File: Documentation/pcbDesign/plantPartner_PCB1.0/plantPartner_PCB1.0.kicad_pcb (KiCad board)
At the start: 2 copper layers, 1 part, among them U1 ESP32-WROOM-32

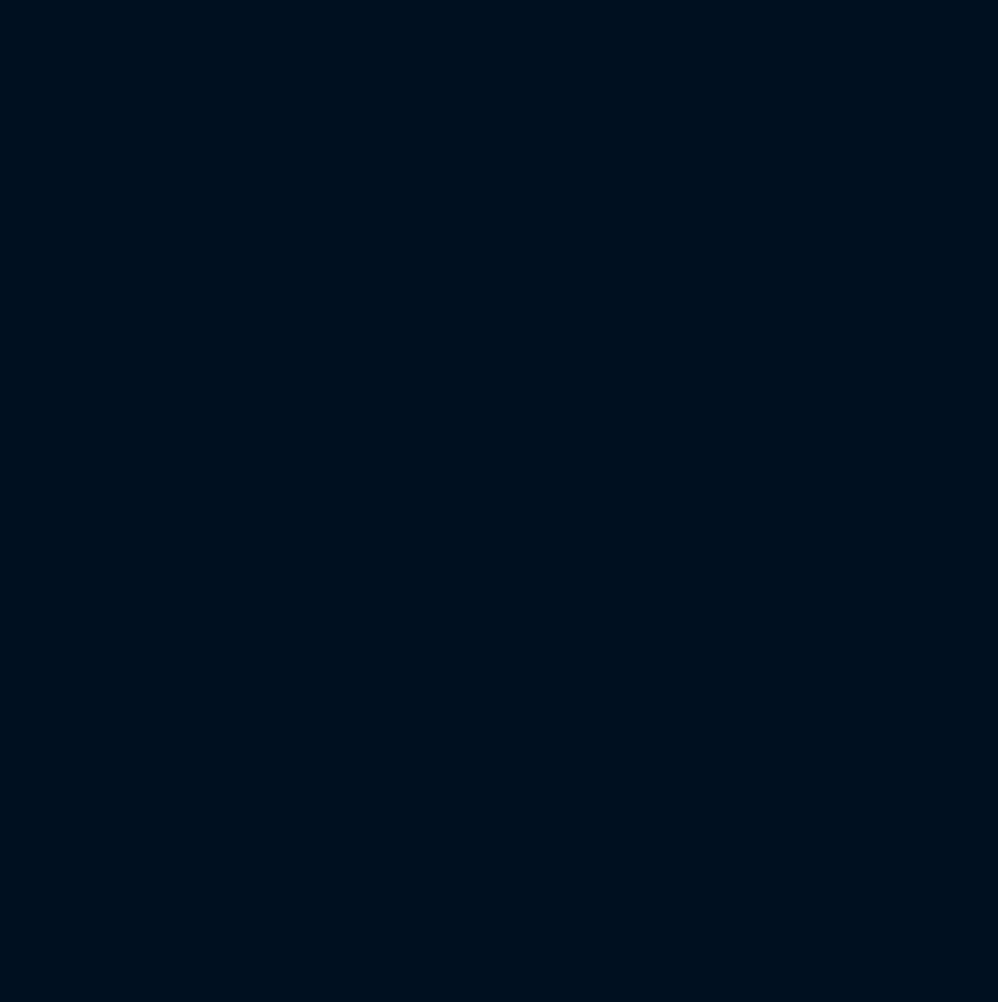
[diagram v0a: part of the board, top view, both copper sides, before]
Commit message: Verified the Schematic designs for the RS-485 Transceiver and Buck Converter. I will verify the 5V Relay next and then start routing the PCB itself ASAP
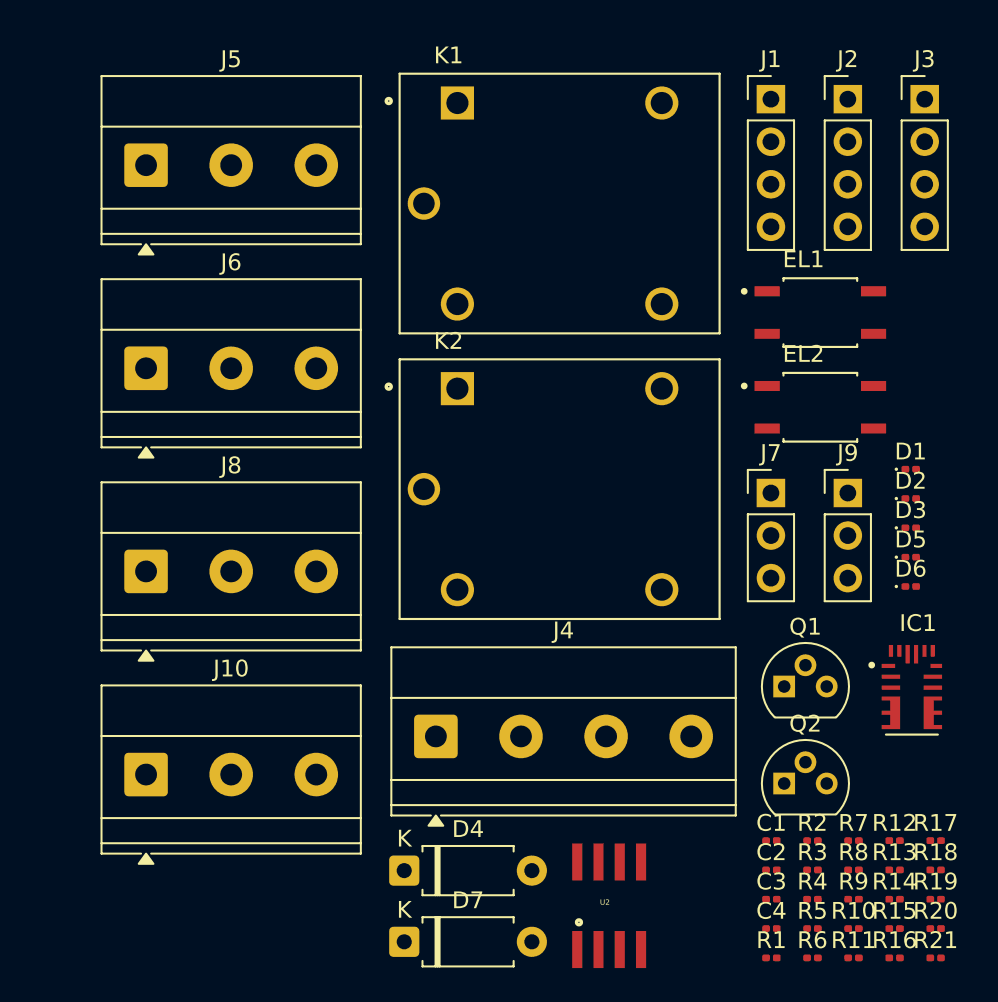
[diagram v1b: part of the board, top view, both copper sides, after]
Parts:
- added C1: 22uF, Capacitor_SMD:C_0201_0603Metric, F.Cu at (163.4, 86.0)
- added C2: 22uF, Capacitor_SMD:C_0201_0603Metric, F.Cu at (163.4, 87.8)
- added C3: 10uF, Capacitor_SMD:C_0201_0603Metric, F.Cu at (163.4, 89.5)
- added C4: 0.1uF, Capacitor_SMD:C_0201_0603Metric, F.Cu at (163.4, 91.2)
- added D1: LED, LED_SMD:LED_0201_0603Metric, F.Cu at (171.7, 63.8)
- added D2: LED, LED_SMD:LED_0201_0603Metric, F.Cu at (171.7, 65.6)
- added D3: LED, LED_SMD:LED_0201_0603Metric, F.Cu at (171.7, 67.3)
- added D4: 1N400x, Diode_THT:D_A-405_P7.62mm_Horizontal, F.Cu at (141.4, 87.8)
- added D5: LED, LED_SMD:LED_0201_0603Metric, F.Cu at (171.7, 69.1)
- added D6: LED, LED_SMD:LED_0201_0603Metric, F.Cu at (171.7, 70.8)
- added D7: 1N400x, Diode_THT:D_A-405_P7.62mm_Horizontal, F.Cu at (141.4, 92.0)
- added EL1: ~, MyCustomFootprints:OPTO_EL357N-G, F.Cu at (166.3, 54.5)
- added EL2: ~, MyCustomFootprints:OPTO_EL357N-G, F.Cu at (166.3, 60.1)
- added IC1: MPM3610, MyCustomFootprints:CONV_MPM3610GQV-P, F.Cu at (171.7, 77.1)
- added J1: Conn_01x04, Connector_PinHeader_2.54mm:PinHeader_1x04_P2.54mm_Vertical, F.Cu at (163.3, 41.7)
- added J10: Screw_Terminal, TerminalBlock_Phoenix:TerminalBlock_Phoenix_MKDS-1,5-3-5.08_1x03_P5.08mm_Horizontal, F.Cu at (126.0, 82.1)
- added J2: Conn_01x04, Connector_PinHeader_2.54mm:PinHeader_1x04_P2.54mm_Vertical, F.Cu at (167.9, 41.7)
- added J3: Conn_01x04, Connector_PinHeader_2.54mm:PinHeader_1x04_P2.54mm_Vertical, F.Cu at (172.5, 41.7)
- added J4: Screw_Terminal, TerminalBlock_Phoenix:TerminalBlock_Phoenix_MKDS-1,5-4-5.08_1x04_P5.08mm_Horizontal, F.Cu at (143.3, 79.8)
- added J5: Screw_Terminal, TerminalBlock_Phoenix:TerminalBlock_Phoenix_MKDS-1,5-3-5.08_1x03_P5.08mm_Horizontal, F.Cu at (126.0, 45.7)
- added J6: Screw_Terminal, TerminalBlock_Phoenix:TerminalBlock_Phoenix_MKDS-1,5-3-5.08_1x03_P5.08mm_Horizontal, F.Cu at (126.0, 57.8)
- added J7: Conn_01x03, Connector_PinHeader_2.54mm:PinHeader_1x03_P2.54mm_Vertical, F.Cu at (163.3, 65.2)
- added J8: Screw_Terminal, TerminalBlock_Phoenix:TerminalBlock_Phoenix_MKDS-1,5-3-5.08_1x03_P5.08mm_Horizontal, F.Cu at (126.0, 69.9)
- added J9: Conn_01x03, Connector_PinHeader_2.54mm:PinHeader_1x03_P2.54mm_Vertical, F.Cu at (167.9, 65.2)
- added K1: SRD-05VDC-SL-C, MyCustomFootprints:RELAY_SRD-05VDC-SL-C, F.Cu at (150.7, 48.0)
- added K2: SRD-05VDC-SL-C, MyCustomFootprints:RELAY_SRD-05VDC-SL-C, F.Cu at (150.7, 65.0)
- added Q1: PNP, Package_TO_SOT_THT:TO-92, F.Cu at (164.1, 76.8)
- added Q2: PNP, Package_TO_SOT_THT:TO-92, F.Cu at (164.1, 82.6)
- added R1: 100k, Resistor_SMD:R_0201_0603Metric, F.Cu at (163.4, 93.0)
- added R10: 20k, Resistor_SMD:R_0201_0603Metric, F.Cu at (168.3, 91.2)
- added R11: 120, Resistor_SMD:R_0201_0603Metric, F.Cu at (168.3, 93.0)
- added R12: 1k, Resistor_SMD:R_0201_0603Metric, F.Cu at (170.7, 86.0)
- added R13: 500, Resistor_SMD:R_0201_0603Metric, F.Cu at (170.7, 87.8)
- added R14: 10k, Resistor_SMD:R_0201_0603Metric, F.Cu at (170.7, 89.5)
- added R15: 470, Resistor_SMD:R_0201_0603Metric, F.Cu at (170.7, 91.2)
- added R16: 1k, Resistor_SMD:R_0201_0603Metric, F.Cu at (170.7, 93.0)
- added R17: 1k, Resistor_SMD:R_0201_0603Metric, F.Cu at (173.2, 86.0)
- added R18: 500, Resistor_SMD:R_0201_0603Metric, F.Cu at (173.2, 87.8)
- added R19: 10k, Resistor_SMD:R_0201_0603Metric, F.Cu at (173.2, 89.5)
- added R2: 100k, Resistor_SMD:R_0201_0603Metric, F.Cu at (165.8, 86.0)
- added R20: 470, Resistor_SMD:R_0201_0603Metric, F.Cu at (173.2, 91.2)
- added R21: 1k, Resistor_SMD:R_0201_0603Metric, F.Cu at (173.2, 93.0)
- added R3: 18.7k, Resistor_SMD:R_0201_0603Metric, F.Cu at (165.8, 87.8)
- added R4: 10k, Resistor_SMD:R_0201_0603Metric, F.Cu at (165.8, 89.5)
- added R5: 10k, Resistor_SMD:R_0201_0603Metric, F.Cu at (165.8, 91.2)
- added R6: 10k, Resistor_SMD:R_0201_0603Metric, F.Cu at (165.8, 93.0)
- added R7: 10k, Resistor_SMD:R_0201_0603Metric, F.Cu at (168.3, 86.0)
- added R8: 1k, Resistor_SMD:R_0201_0603Metric, F.Cu at (168.3, 87.8)
- added R9: 20k, Resistor_SMD:R_0201_0603Metric, F.Cu at (168.3, 89.5)
- added U2: MAX485, MyCustomFootprints:SO08, F.Cu at (153.7, 89.9)
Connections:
- net Net-(U1-GND-Pad1) renamed GND
- U1 pad 14: unconnected-(U1-IO12-Pad14) -> /PWM_MOTOR_PIN
- U1 pad 2: unconnected-(U1-VDD-Pad2) -> 12V
- U1 pad 33: unconnected-(U1-IO21-Pad33) -> /DE
- U1 pad 36: unconnected-(U1-IO22-Pad36) -> /RO
- U1 pad 37: unconnected-(U1-IO23-Pad37) -> /DI
- U1 pad 4: unconnected-(U1-SENSOR_VP-Pad4) -> /ADC_LIGHT_SENSOR
- U1 pad 5: unconnected-(U1-SENSOR_VN-Pad5) -> /ADC_MOISTURE_SENSOR

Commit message: Since I was able to copy the Buck Converter and RS-485 Relay verbatim from an online source, verifying them was rather quick but for this 5V relay I am trying to properly simulate and probe its voltage values. I started with KiCad's sim and that was bad so then I moved into LTspice and asked ChatGPT to help convert some of the components to standard SPICE parts since I only took Circuits 1. I am making progress but it's not feeling like it lol
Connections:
- IC1 pad 11: unconnected-(IC1-BST-Pad11) -> /BST
- J1 pad 2: VIN -> 12V
- U1 pad 36: /RO -> Net-(U1-IO22)
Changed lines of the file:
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@@
 	(net 43 "/FB")
 	(net 44 "/SW")
-	(net 45 "unconnected-(IC1-BST-Pad11)")
+	(net 45 "/BST")
 	(net 46 "VCC")
 	(net 47 "unconnected-(IC1-AAM-Pad18)")
-	(net 48 "VIN")
+	(net 48 "Net-(U1-IO22)")
 	(net 49 "/DI")
 	(net 50 "/RO")
@@
 			(size 1.1 0.25)
 			(layers "F.Cu" "F.Mask" "F.Paste")
-			(net 45 "unconnected-(IC1-BST-Pad11)")
+			(net 45 "/BST")
 			(pinfunction "BST")
 			(pintype "passive")
@@
 			(size 1.5 0.9)
 			(layers "F.Cu" "F.Mask" "F.Paste")
-			(net 50 "/RO")
+			(net 48 "Net-(U1-IO22)")
 			(pinfunction "IO22")
 			(pintype "bidirectional")
@@
 			(layers "*.Cu" "*.Mask")
 			(remove_unused_layers no)
-			(net 48 "VIN")
+			(net 1 "12V")
 			(pinfunction "Pin_2")
 			(pintype "passive")

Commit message: Verified circuit. Time to finalize Schematic with symbols that have compatible footprints. Need to add remaining 3D models, testing pins for PCB, and verify relay octocoupler footprint + symbol
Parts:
- added R22: 1k, Resistor_SMD:R_0201_0603Metric, F.Cu at (152.2, 109.0)
- IC1: footprint MyCustomFootprints:CONV_MPM3610GQV-P -> MyCustomFootprints:MPM3610
- moved EL1 22.8 mm to (189.0, 52.5)
- moved EL2 22.7 mm to (189.0, 61.0)
- moved C1 21.1 mm to (182.7, 94.5)
- moved C2 21.1 mm to (182.7, 96.2)
- moved C3 21.1 mm to (182.7, 98.0)
- moved C4 21.1 mm to (182.7, 99.8)
- moved R1 21.1 mm to (182.7, 101.5)
- moved R10 21.1 mm to (187.6, 99.8)
- moved R11 21.1 mm to (187.6, 101.5)
- moved R7 21.1 mm to (187.6, 94.5)
- moved R8 21.1 mm to (187.6, 96.2)
- moved R9 21.1 mm to (187.6, 98.0)
- moved R12 21.1 mm to (190.0, 94.5)
- moved R13 21.1 mm to (190.0, 96.2)
- moved R14 21.1 mm to (190.0, 98.0)
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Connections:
- net /PWM_MOTOR_PIN renamed /PWM_WATER_PIN
- IC1 pad 18: unconnected-(IC1-AAM-Pad18) -> /AAM
- U1 pad 16: unconnected-(U1-IO13-Pad16) -> /PWM_FERTIL_PIN

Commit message: Added the small circuitry needed for ADC sensors, ESP-32 External LED, Overall PCB Heartbeat sensor. Fixed wiring issue with 5V Relays. Met with Prof. Alex about our Alpha Build status. I tried to add new optocoupler symbol and footprint but KiCad could not find it for some reason (rip). Now I need to add used ESP-32 pins, extra 5V and 12V pins, extra GND pins, and unused ESP32 Pins, THEN finally I can route (I hope … please lol).
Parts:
- removed U1: ESP32-WROOM-32, RF_Module:ESP32-WROOM-32
- added D10: LED, LED_SMD:LED_0201_0603Metric, F.Cu at (346.3, 94.5)
- added D8: SS14, Diode_SMD:D_SMA, F.Cu at (132.0, 117.4)
- added D9: SS14, Diode_SMD:D_SMA, F.Cu at (132.0, 121.9)
- added J11: Conn_01x04, Connector_PinHeader_2.54mm:PinHeader_1x04_P2.54mm_Vertical, F.Cu at (155.8, 103.7)
- added J12: Conn_01x03, Connector_PinHeader_2.54mm:PinHeader_1x03_P2.54mm_Vertical, F.Cu at (120.7, 107.7)
- added J13: Conn_01x03, Connector_PinHeader_2.54mm:PinHeader_1x03_P2.54mm_Vertical, F.Cu at (125.3, 107.7)
- added J14: Conn_01x03, Connector_PinHeader_2.54mm:PinHeader_1x03_P2.54mm_Vertical, F.Cu at (129.8, 107.7)
- added J15: Conn_01x03, Connector_PinHeader_2.54mm:PinHeader_1x03_P2.54mm_Vertical, F.Cu at (134.4, 107.7)
- added J16: Conn_01x04, Connector_PinHeader_2.54mm:PinHeader_1x04_P2.54mm_Vertical, F.Cu at (160.4, 103.7)
- added J18: Screw_Terminal_01x02, TerminalBlock_Phoenix:TerminalBlock_Phoenix_MKDS-1,5-2-5.08_1x02_P5.08mm_Horizontal, F.Cu at (112.8, 121.3)
- added J19: Barrel_Jack, Connector_BarrelJack:BarrelJack_GCT_DCJ200-10-A_Horizontal, F.Cu at (168.2, 103.4)
- added R23: 1k, Resistor_SMD:R_0201_0603Metric, F.Cu at (165.6, 94.9)
- added R24: 1k, Resistor_SMD:R_0201_0603Metric, F.Cu at (343.7, 96.2)
- added R26: 1k, Resistor_SMD:R_0201_0603Metric, F.Cu at (343.7, 98.0)
- added U3: ESP32-DEVKIT-V1, MyCustomFootprints:MODULE_ESP32_DEVKIT_V1, F.Cu at (124.7, 79.2)
- moved R22 192.0 mm to (343.7, 94.5)
- moved J9 67.0 mm to (116.1, 107.7)
- moved J7 67.0 mm to (111.5, 107.7)
- moved J1 65.5 mm to (142.0, 103.7)
- moved J2 65.5 mm to (146.6, 103.7)
- moved J3 65.5 mm to (151.2, 103.7)
- moved Q1 58.2 mm to (123.4, 118.3)
- moved Q2 58.2 mm to (123.4, 124.1)
- moved D1 45.1 mm to (176.5, 108.7)
- moved D2 45.1 mm to (176.5, 110.4)
- moved D3 45.1 mm to (176.5, 112.2)
- moved D5 45.1 mm to (176.5, 113.9)
- moved D6 45.1 mm to (176.5, 115.7)
- moved EL1 41.0 mm to (172.1, 89.8)
- moved J4 40.1 mm to (143.3, 119.9)
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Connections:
- IC1 pad 2: VCC -> 12V
- J7 pad 3: /DC+ -> 12V
- J9 pad 3: /DC+ -> 12V
- K1 pad NC: /NC -> 12V
- K2 pad NC: /NC -> 12V
- Q1 pad 3: /DC+ -> 12V
- Q2 pad 3: /DC+ -> 12V
- R12 pad 1: /DC+ -> 12V
- R14 pad 1: /DC+ -> 12V
- R17 pad 1: /DC+ -> 12V
- R19 pad 1: /DC+ -> 12V
- R22 pad 2: /RO -> /EXTERNAL LED

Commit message: Fixed optocoupler for Relay circuits
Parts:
- removed EL1, EL2: ~, MyCustomFootprints:OPTO_EL357N-G
- removed J8: Screw_Terminal, TerminalBlock_Phoenix:TerminalBlock_Phoenix_MKDS-1,5-3-5.08_1x03_P5.08mm_Horizontal
- added D11: LED, LED_SMD:LED_0201_0603Metric, F.Cu at (117.5, 58.4)
- added J17: Conn_01x03, Connector_PinHeader_2.54mm:PinHeader_1x03_P2.54mm_Vertical, F.Cu at (114.8, 66.7)
- added U1: EL357N-G, MyCustomFootprints:OPTO_EL357N-G, F.Cu at (59.7, 85.6)
- added U4: EL357N-G, MyCustomFootprints:OPTO_EL357N-G, F.Cu at (59.7, 91.3)
- J10, J6: value Screw_Terminal -> Screw_Terminal_01x03
- J5: value Screw_Terminal -> Conn_01x02; footprint TerminalBlock_Phoenix:TerminalBlock_Phoenix_MKDS-1,5-3-5.08_1x03_P5.08mm_Horizontal -> Connector_PinHeader_2.54mm:PinHeader_1x02_P2.54mm_Vertical
- moved R22 233.2 mm to (114.8, 49.7)
- moved R24 232.8 mm to (114.8, 53.2)
- moved R26 232.8 mm to (114.8, 54.9)
- moved D10 231.9 mm to (117.5, 56.7)
- moved U2 112.5 mm to (67.3, 95.5)
- moved D4 104.5 mm to (66.0, 84.9)
- moved D7 104.5 mm to (66.0, 89.2)
- moved IC1 100.1 mm to (77.8, 95.2)
- moved J19 90.8 mm to (111.8, 32.3)
- moved D1 84.7 mm to (117.5, 47.9)
- moved D2 84.7 mm to (117.5, 49.7)
- moved D3 84.7 mm to (117.5, 51.4)
- moved D5 84.7 mm to (117.5, 53.2)
- moved D6 84.7 mm to (117.5, 54.9)
- moved J5 78.7 mm to (72.5, 93.6)
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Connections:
- J10 pad 1: /NO -> GND
- J10 pad 2: /COM -> /NO
- J10 pad 3: /NC -> /COM
- J5 pad 1: 12V -> /ADC_LIGHT_SENSOR
- J5 pad 2: GND -> 12V
- J6 pad 1: /NO -> GND
- J6 pad 2: /COM -> /NO
- J6 pad 3: /NC -> /COM

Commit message: Finished adding Testing Pins. Starting Routing by drawing it out and organizing components in PCB. Quickly realized that I incorrectly setup 5V and 12V labels so will need to re-label those soon
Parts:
- added J20: Conn_02x04_Top_Bottom, Connector_PinHeader_2.54mm:PinHeader_2x04_P2.54mm_Vertical, F.Cu at (222.5, 55.4)
- added J21: Conn_01x04, Connector_PinHeader_2.54mm:PinHeader_1x04_P2.54mm_Vertical, F.Cu at (223.5, 41.0)
- added J22: Conn_01x04, Connector_PinHeader_2.54mm:PinHeader_1x04_P2.54mm_Vertical, F.Cu at (136.8, 132.0)
- added J23: Conn_01x02, Connector_PinHeader_2.54mm:PinHeader_1x02_P2.54mm_Vertical, F.Cu at (195.0, 45.0)
- added J24: Conn_01x04, Connector_PinHeader_2.54mm:PinHeader_1x04_P2.54mm_Vertical, F.Cu at (274.6, 22.5)
- added J25: Conn_01x04, Connector_PinHeader_2.54mm:PinHeader_1x04_P2.54mm_Vertical, F.Cu at (231.5, 41.0)
- added J26: Conn_01x01, Connector_PinHeader_2.54mm:PinHeader_1x01_P2.54mm_Vertical, F.Cu at (275.0, 111.0)
- added J27: Conn_01x03, Connector_PinHeader_2.54mm:PinHeader_1x03_P2.54mm_Vertical, F.Cu at (55.0, 109.0)
- added J8: Conn_02x04_Top_Bottom, Connector_PinHeader_2.54mm:PinHeader_2x04_P2.54mm_Vertical, F.Cu at (39.0, 138.2)
- moved U4 213.9 mm to (273.5, 85.5)
- moved D4 182.7 mm to (248.7, 80.0)
- moved K2 177.6 mm to (268.5, 98.0)
- moved J13 155.2 mm to (255.0, 86.4)
- moved J12 154.8 mm to (250.0, 86.5)
- moved J9 154.8 mm to (245.4, 86.5)
- moved Q2 152.6 mm to (262.5, 85.5)
- moved J5 135.1 mm to (195.0, 36.5)
- moved R21 134.7 mm to (245.3, 81.8)
- moved R17 134.2 mm to (245.2, 74.5)
- moved R18 134.2 mm to (245.2, 76.2)
- moved R19 134.2 mm to (245.2, 78.0)
- moved R20 134.2 mm to (245.2, 79.8)
- moved D5 128.3 mm to (240.4, 90.0)
- moved D6 128.3 mm to (240.4, 91.8)
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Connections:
- C1 pad 1: 12V -> +5V
- IC1 pad 7: 12V -> +5V
- IC1 pad 8: 12V -> +5V
- IC1 pad 9: 12V -> +5V
- J1 pad 3: 12V -> +5V
- J12 pad 3: 12V -> +5V
- J14 pad 3: 12V -> +5V
- J16 pad 2: 12V -> +5V
- J17 pad 2: 12V -> +5V
- J5 pad 2: 12V -> +5V
- J7 pad 3: 12V -> +5V
- J9 pad 3: 12V -> +5V
- Q1 pad 3: 12V -> +5V
- Q2 pad 3: 12V -> +5V
- R12 pad 1: 12V -> +5V
- R14 pad 1: 12V -> +5V
- R17 pad 1: 12V -> +5V
- R19 pad 1: 12V -> +5V
- R2 pad 1: 12V -> +5V
- R26 pad 1: 12V -> +5V
- U3 pad 1: unconnected-(U3-3V3-Pad1) -> /ESP_3.3V
- U3 pad 10: unconnected-(U3-D19-Pad10) -> /MISO/VSPI_MISO
- U3 pad 12: unconnected-(U3-RX0-Pad12) -> /RX0
- U3 pad 13: unconnected-(U3-TX0-Pad13) -> /TX0
- U3 pad 14: unconnected-(U3-D22-Pad14) -> /SCL
- U3 pad 15: unconnected-(U3-D23-Pad15) -> /MOSI
- U3 pad 16: unconnected-(U3-EN-Pad16) -> /ESP_EN
- U3 pad 19: unconnected-(U3-D34-Pad19) -> /ADC1_6
- U3 pad 20: /TEMP SWITCH -> /ADC1_7
- U3 pad 21: unconnected-(U3-D32-Pad21) -> /ADC1_4/Touch9
- U3 pad 22: unconnected-(U3-D33-Pad22) -> /ADC1_5/Touch8
- U3 pad 23: unconnected-(U3-D25-Pad23) -> /ADC2_8/DAC1
- U3 pad 24: unconnected-(U3-D26-Pad24) -> /ADC2_9/DAC2
- U3 pad 25: unconnected-(U3-D27-Pad25) -> /ADC2_7/Touch7
- U3 pad 3: unconnected-(U3-D15-Pad3) -> /<NO NET>
- U3 pad 30: 12V -> +5V
- U3 pad 5: unconnected-(U3-D4-Pad5) -> /ADC2_0/Touch0
- U3 pad 8: unconnected-(U3-D5-Pad8) -> /VSPI_CS
- U3 pad 9: unconnected-(U3-D18-Pad9) -> /SCK/VSPI_CLK
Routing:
- net GND: track 0.00 -> 32.9 mm
- net 12V: track 0.00 -> 24.9 mm
- net /12V_SCREW: track 0.00 -> 7.50 mm
- net /12V_JACK: track 0.00 -> 3.25 mm
- net Net-(U3-RX2): track 0.00 -> 2.40 mm
- net /ADC_LIGHT_SENSOR: track 0.00 -> 2.28 mm
- net Net-(D11-A): track 0.00 -> 0.95 mm
- net +5V: track 0.00 -> 0.91 mm
- net /FB: track 0.00 -> 0.87 mm
- net /EN: track 0.00 -> 0.74 mm
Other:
- board outline added: 271 x 152 mm

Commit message: We showed off the Alpha Build to Tyler and I worked on the PCB Routing. I am trying to resolve the Electrical Rules Checker (ERC) now while routing.
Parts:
- moved J4 27.2 mm to (53.8, 48.0)
- moved R11 26.5 mm to (32.8, 31.0), turned to 90 degrees
- moved R16 24.5 mm to (40.8, 120.8)
- moved J11 23.5 mm to (20.2, 40.2)
- moved R10 23.2 mm to (32.0, 31.0), turned to 90 degrees
- moved R9 22.9 mm to (32.8, 32.4), turned to -90 degrees
- moved R8 20.6 mm to (38.5, 42.3)
- moved J2 19.8 mm to (46.0, 28.0)
- moved C3 16.7 mm to (33.7, 43.6)
- moved C4 16.7 mm to (33.7, 45.4)
- moved D1 16.7 mm to (38.5, 43.1)
- moved J3 13.2 mm to (28.0, 35.6), turned to 180 degrees
- moved R4 11.9 mm to (41.4, 32.6), turned to -90 degrees
- moved R6 9.43 mm to (41.5, 30.8), turned to 90 degrees
- moved R5 9.41 mm to (42.2, 30.7), turned to 90 degrees
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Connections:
- C2 pad 1: 12V -> +12V
- C3 pad 1: 12V -> +12V
- C4 pad 1: 12V -> +12V
- D8 pad 1: 12V -> +12V
- D9 pad 1: 12V -> +12V
- IC1 pad 16: 12V -> +12V
- IC1 pad 2: 12V -> +12V
- J1 pad 2: 12V -> +12V
- J11 pad 3: 12V -> +12V
- J12 pad 1: 12V -> +12V
- J13 pad 3: 12V -> +12V
- J14 pad 1: 12V -> +12V
- J15 pad 3: 12V -> +12V
- J16 pad 3: 12V -> +12V
- J21 pad 3: 12V -> +12V
- J22 pad 3: 12V -> +12V
- J26 pad 1: 12V -> +12V
- J27 pad 1: 12V -> +12V
- J3 pad 1: 12V -> +12V
- J4 pad 3: 12V -> +12V
- K1 pad NC: 12V -> +12V
- K2 pad NC: 12V -> +12V
- R1 pad 1: 12V -> +12V
- R10 pad 1: 12V -> +12V
- R4 pad 1: 12V -> +12V
- R5 pad 1: 12V -> +12V
- R6 pad 1: 12V -> +12V
- R7 pad 1: 12V -> +12V
- R8 pad 1: 12V -> +12V
- U1 pad 2: 12V -> +12V
- U2 pad 8: 12V -> +12V
- U3 pad 27: 12V -> +12V
- U3 pad 28: 12V -> +12V
- U4 pad 2: 12V -> +12V
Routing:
- net +12V: track 0.00 -> 26.9 mm
- net 12V: track 24.9 -> 0.00 mm
- net /DE: track 0.00 -> 8.75 mm
- net /RO: track 0.00 -> 7.26 mm
- net /DI: track 0.00 -> 6.59 mm
- net /B: track 0.00 -> 2.79 mm
- net /A: track 0.00 -> 2.76 mm
- net Net-(D1-A): track 0.00 -> 0.81 mm
